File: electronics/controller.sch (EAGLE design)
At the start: 9 parts, among them IC2 L293D

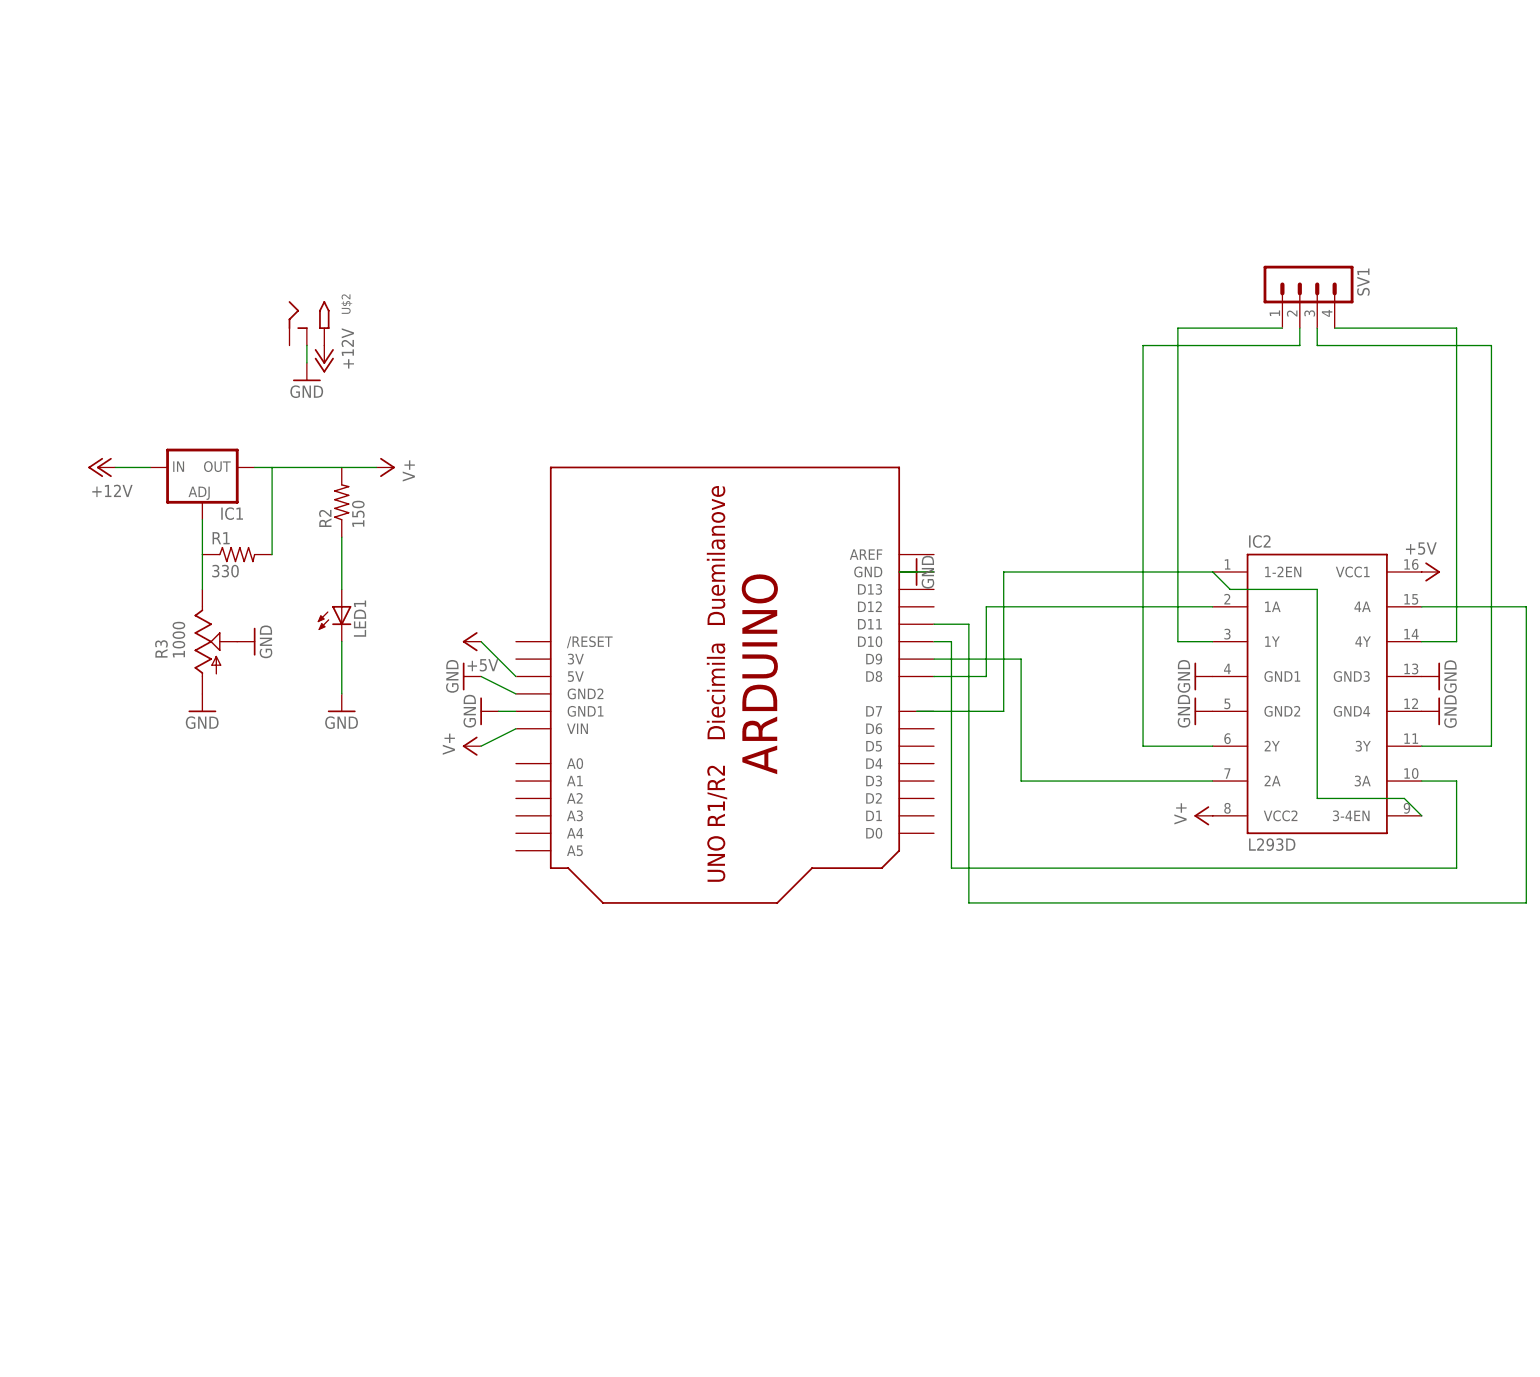
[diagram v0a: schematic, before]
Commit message: Updated #robogarden manual control code and schematic
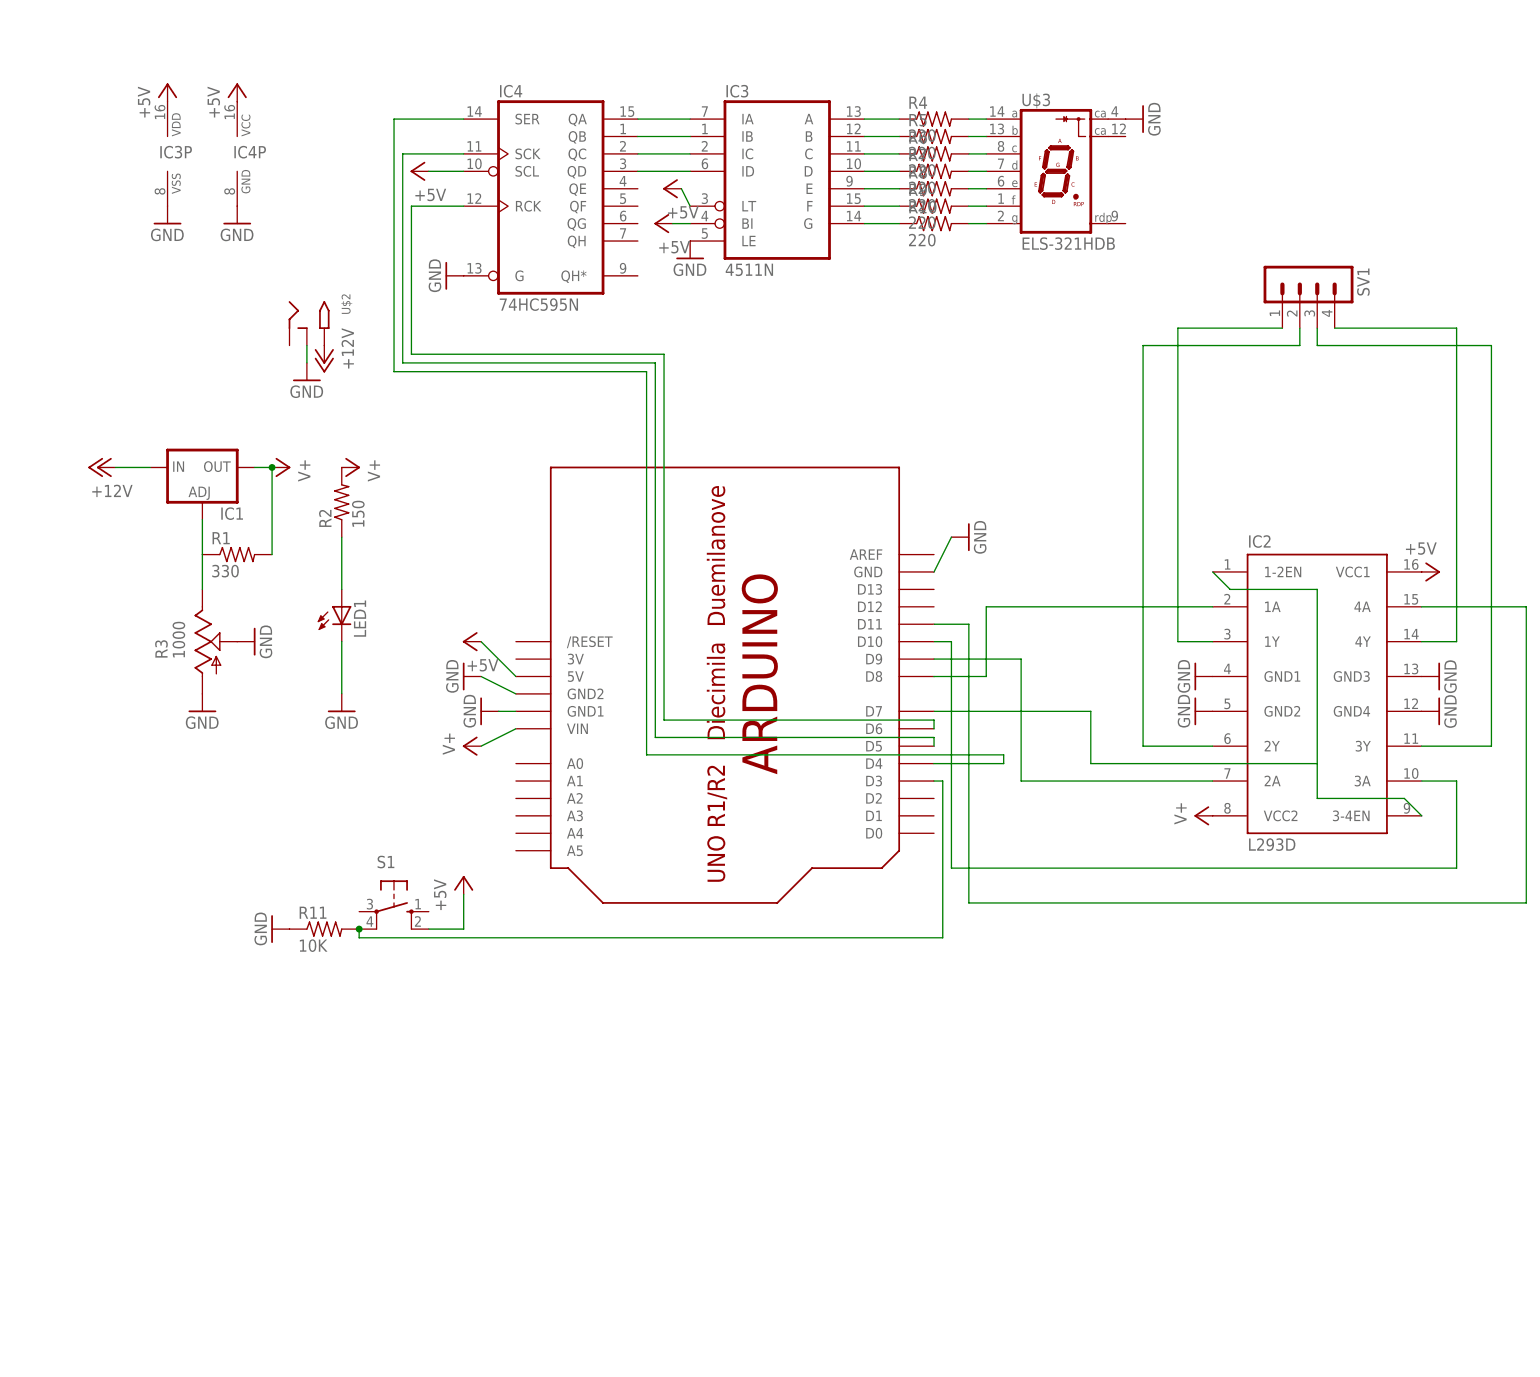
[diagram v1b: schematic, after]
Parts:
- added IC3: 4511N, 45xx:4511N
- added IC4: 74HC595N, 74xx-eu:74HC595N
- added R10, R4, R5, R6, R7, R8, R9: 220, adafruit:R-US_0207/7
- added R11: 10K, adafruit:R-US_0207/7
- added S1: (no value), switch-omron:10-XX
- added U$3: ELS-321HDB, national-semiconductor:ELS-321HDB
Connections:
- new net N$13: IC2.1-2EN, IC2.3-4EN, U$1.D7
- new net N$14: IC3A.C, R6.1
- new net N$15: IC3A.D, R7.1
- new net N$16: IC3A.E, R8.1
- new net N$17: IC3A.F, R9.1
- new net N$18: IC3A.G, R10.1
- new net N$19: R4.2, U$3.A
- new net N$20: R5.2, U$3.B
- new net N$21: R6.2, U$3.C
- new net N$22: R7.2, U$3.D
- new net N$23: R8.2, U$3.E
- new net N$24: R9.2, U$3.F
- new net N$25: R10.2, U$3.G
- new net N$26: IC3A.IA, IC4A.QA
- new net N$27: IC3A.IB, IC4A.QB
- new net N$28: IC3A.IC, IC4A.QC
- new net N$29: IC3A.ID, IC4A.QD
- new net N$30: IC4A.SER, U$1.D4
- new net N$31: IC4A.SCK, U$1.D5
- new net N$32: IC4A.RCK, U$1.D6
- new net N$34: R11.2, S1.P1, U$1.D3
- net +5V: now also IC3A.BI, IC3A.LT, IC3P.VDD, IC4A.SCL, IC4P.VCC, S1.S1
- net GND: now also IC3A.LE, IC3P.VSS, IC4A.G, IC4P.GND, R11.1, U$3.C@1
- net N$12: now also IC3A.B, R5.1; no longer IC2.1-2EN, IC2.3-4EN
- net N$2: now also IC3A.A, R4.1; no longer IC1.OUT, R1.2, R2.2
- net V+: now also IC1.OUT, R1.2, R2.2

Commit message: Updated #RoboGarden code with homing check, refactored the codebase to be cleaner with better comments and variable names, changed logic on button press
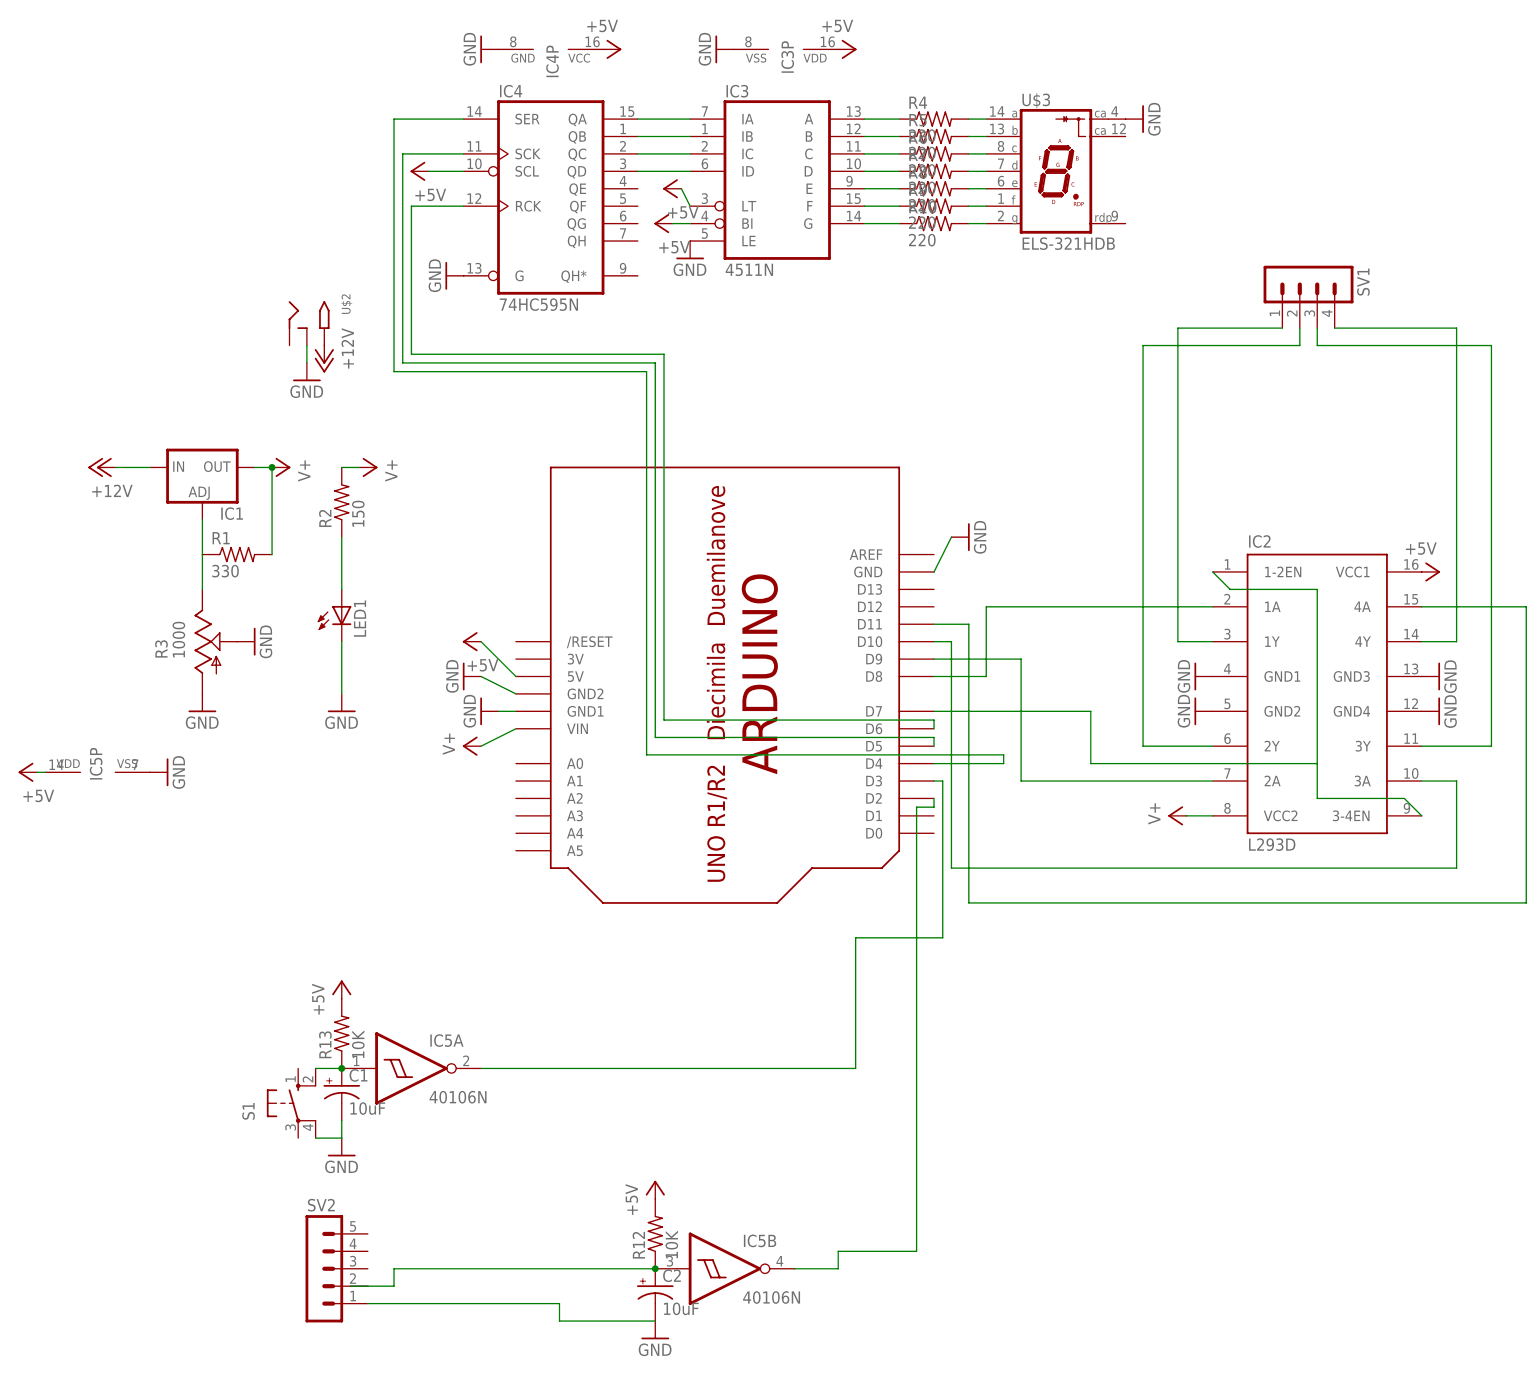
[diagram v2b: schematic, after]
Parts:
- removed R11: 10K, adafruit:R-US_0207/7
- added C1, C2: 10uF, rcl:CPOL-USE2.5-5
- added IC5: 40106N, 40xx:40106N
- added R12, R13: 10K, adafruit:R-US_0207/7
- added SV2: (no value), con-lstb:MA05-1
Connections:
- new net N$33: C1.+, IC5A.I, R13.1, S1.S1
- new net N$35: C2.+, IC5B.I, R12.1, SV2.2
- new net N$38: IC5B.O, U$1.D2
- net +5V: now also IC5P.VDD, R12.2, R13.2; no longer S1.S1
- net GND: now also C1.-, C2.-, IC5P.VSS, S1.P1, SV2.1; no longer R11.1
- net N$34: now also IC5A.O; no longer R11.2, S1.P1
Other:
- moved on the sheet: IC3P, IC4P, S1
